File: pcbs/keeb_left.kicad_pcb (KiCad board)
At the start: 2 copper layers, 135.4 x 115.9 mm, 70 parts

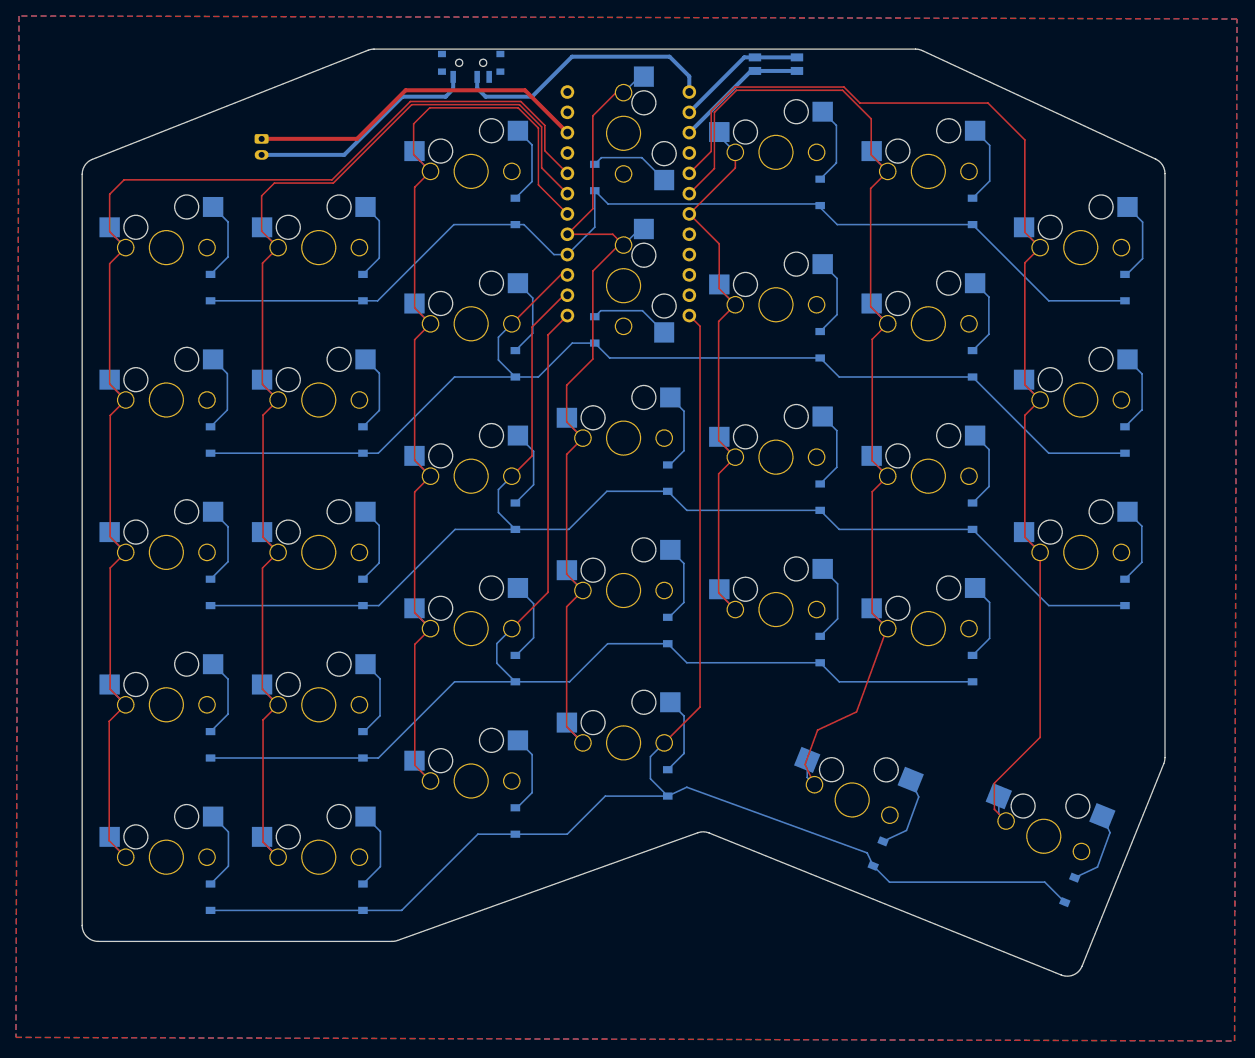
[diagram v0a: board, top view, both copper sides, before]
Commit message: Adding routed right PCB
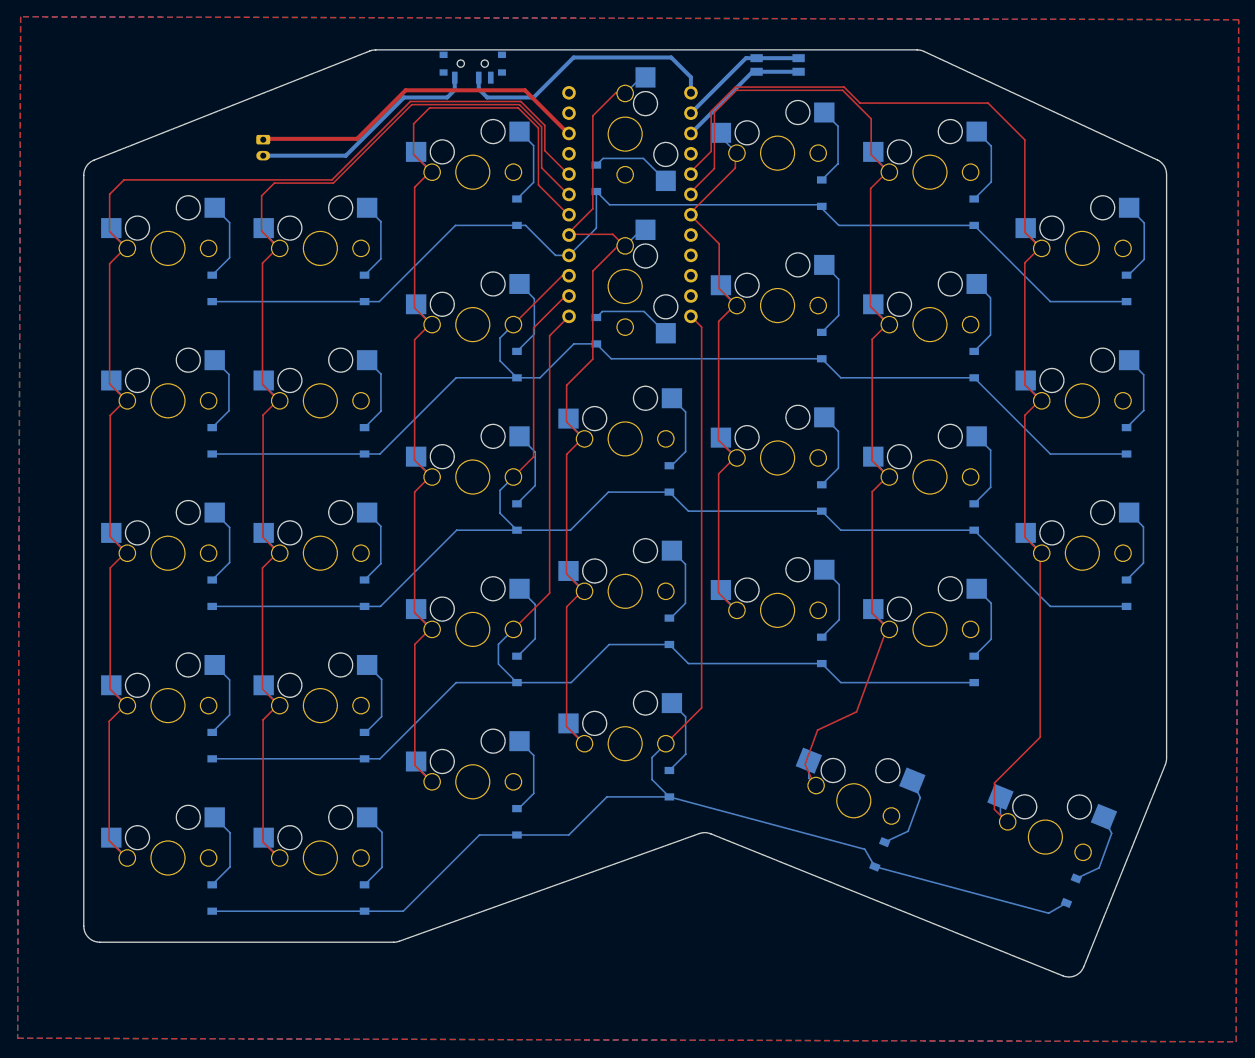
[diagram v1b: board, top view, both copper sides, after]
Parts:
- moved D22 0.23 mm to (178.8, 52.1)
- moved S25 0.23 mm to (192.3, 68.5)
- moved S32 0.23 mm to (182.8, 128.0)
- moved D25 0.23 mm to (197.9, 73.5)
- moved S19 0.23 mm to (173.3, 104.2)
- moved S28 0.23 mm to (211.4, 78.0)
- moved S30 0.23 mm to (154.2, 63.7)
- moved S8 0.23 mm to (116.1, 97.1)
- moved D10 0.23 mm to (121.7, 64.0)
- moved D20 0.23 mm to (178.8, 90.2)
- moved D11 0.23 mm to (140.7, 130.6)
- moved D30 0.23 mm to (186.1, 134.7)
- moved D28 0.23 mm to (216.9, 83.0)
- moved S15 0.23 mm to (135.2, 49.4)
- moved S4 0.23 mm to (97.1, 78.0)
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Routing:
- net P10: track 181.4 -> 180.0 mm

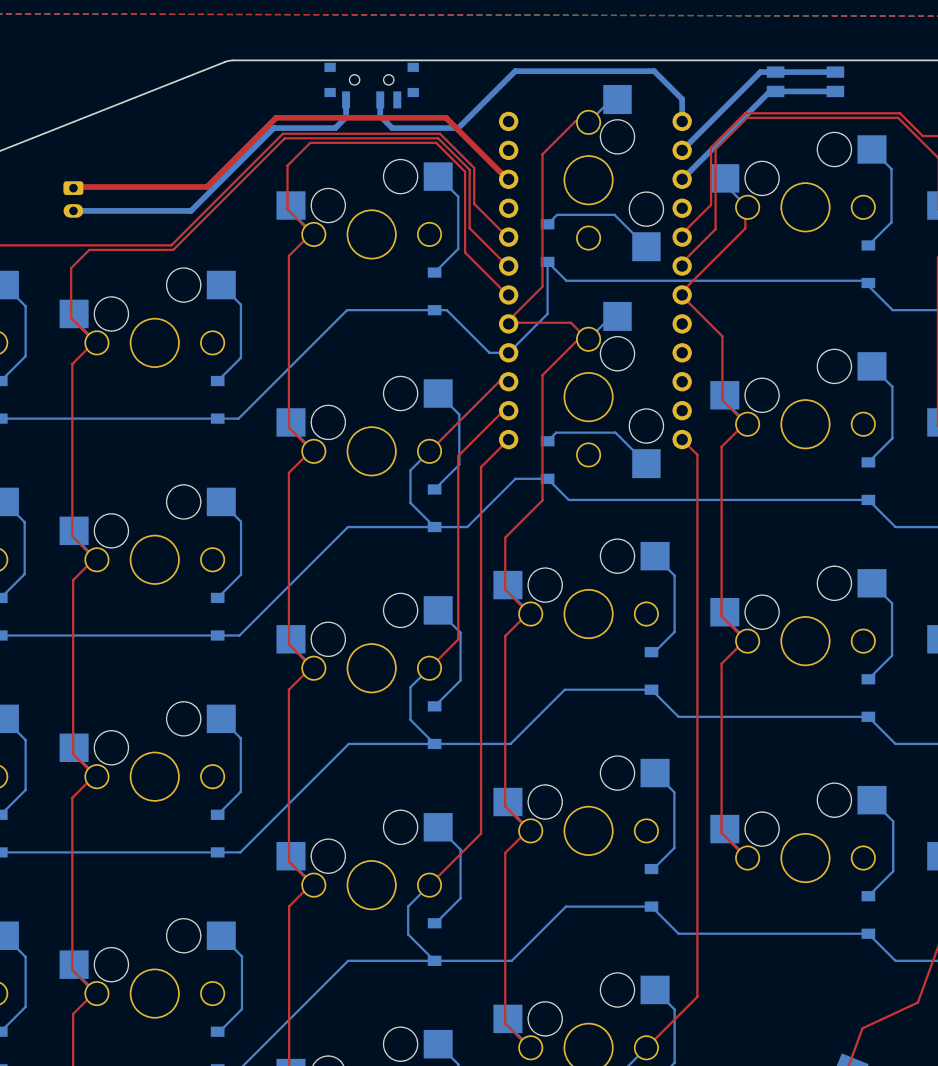
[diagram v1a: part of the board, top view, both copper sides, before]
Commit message: Adding additional outlines for Fusion work, updated MCU placement on PCBs, updated routing to accomodate
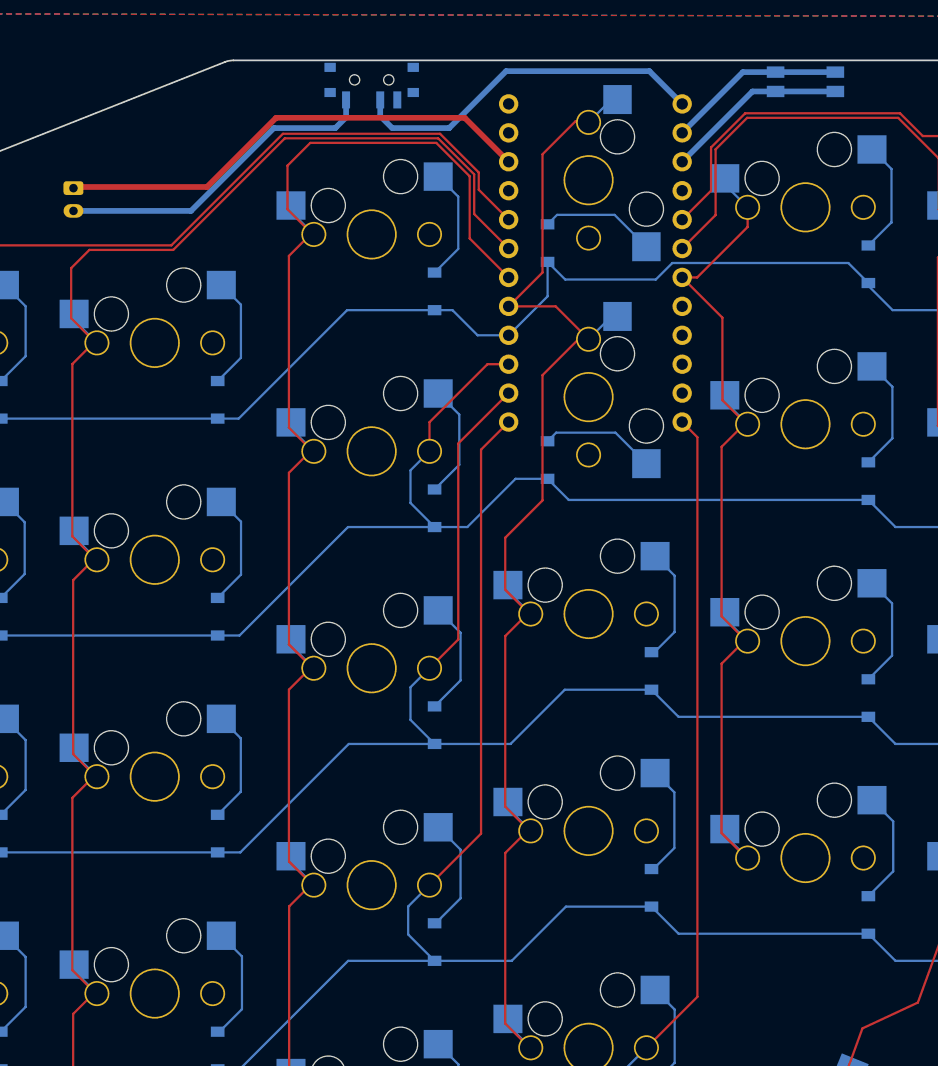
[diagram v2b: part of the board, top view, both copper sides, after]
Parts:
- moved MCU1 1.54 mm to (154.8, 50.7)
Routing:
- net P7: track 143.4 -> 145.5 mm
- net RAW: track 33.4 -> 31.6 mm
- net P10: track 180.0 -> 181.6 mm
- net P9: track 153.5 -> 155.1 mm
- net P20: track 144.1 -> 142.6 mm
- net P21: track 157.8 -> 156.2 mm
- net P4: track 136.1 -> 134.8 mm
- net P2: track 174.7 -> 173.4 mm
- net P3: track 157.3 -> 155.9 mm
- net P8: track 160.1 -> 161.4 mm
- net GND: track 59.2 -> 58.2 mm
- net P6: track 131.6 -> 130.9 mm
- net P19: track 78.9 -> 79.4 mm
